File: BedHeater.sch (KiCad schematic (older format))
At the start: 10 parts, among them J35 Thermistor

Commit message: Finished the schematics wiring and reset the routing.
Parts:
- J35: footprint Connector_PinHeader_2.54mm:PinHeader_1x02_P2.54mm_Vertical -> kicad-molex-sl-footprints:Molex-SL-2POS
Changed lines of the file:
@@
 F 0 "J35" V 4054 4280 50  0000 L CNN
 F 1 "Thermistor" V 4145 4280 50  0000 L CNN
-F 2 "Connector_PinHeader_2.54mm:PinHeader_1x02_P2.54mm_Vertical" H 4050 4200 50  0001 C CNN
+F 2 "kicad-molex-sl-footprints:Molex-SL-2POS" H 4050 4200 50  0001 C CNN
 F 3 "~" H 4050 4200 50  0001 C CNN
 	1    4050 4200

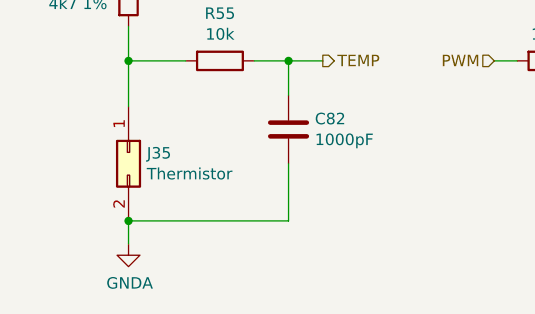
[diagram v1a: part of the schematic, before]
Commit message: Router X and Y drivers (preliminary).
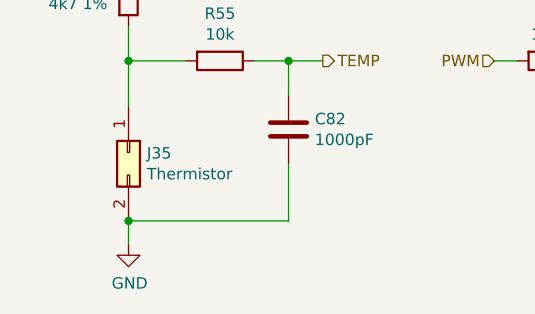
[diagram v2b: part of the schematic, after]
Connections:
- net GNDA is gone; now on net GND: C82.2, J35.2 (Pin_2)
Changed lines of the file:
@@
-$EndComp
-$Comp
-L power:GNDA #PWR?
-U 1 1 5AD4D481
-P 4050 4600
-AR Path="/5AC337B6/5ACBE919/5AD4D269/5AD4D481" Ref="#PWR?"  Part="1"
-AR Path="/5AC337B6/5AD9F95A/5AD4D269/5AD4D481" Ref="#PWR?"  Part="1"
-AR Path="/5AB8F10D/5AD4D481" Ref="#PWR079"  Part="1"
-F 0 "#PWR079" H 4050 4350 50  0001 C CNN
-F 1 "GNDA" H 4055 4427 50  0000 C CNN
-F 2 "" H 4050 4600 50  0001 C CNN
-F 3 "" H 4050 4600 50  0001 C CNN
-	1    4050 4600
-	1    0    0    -1
 $EndComp
 $Comp
@@
 Wire Wire Line
 	6700 3100 6650 3100
+$Comp
+L power:GND #PWR?
+U 1 1 5D3C5293
+P 4050 4600
+F 0 "#PWR?" H 4050 4350 50  0001 C CNN
+F 1 "GND" H 4055 4427 50  0000 C CNN
+F 2 "" H 4050 4600 50  0001 C CNN
+F 3 "" H 4050 4600 50  0001 C CNN
+	1    4050 4600
+	1    0    0    -1
+$EndComp
 $EndSCHEMATC
